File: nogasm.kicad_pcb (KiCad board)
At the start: 2 copper layers, 76.2 x 76.2 mm, 57 parts, among them J1 PJ-031DH 3.5mm, J2 PRT-10811, Q1 BUK92150-55A, Q2 MMBT2222A, Q3 MMBT2222A, Q4 MMBT2222A, SW1 SW_DIP_x04, U1 WS2812B, U10 WS2812B, U11 WS2812B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

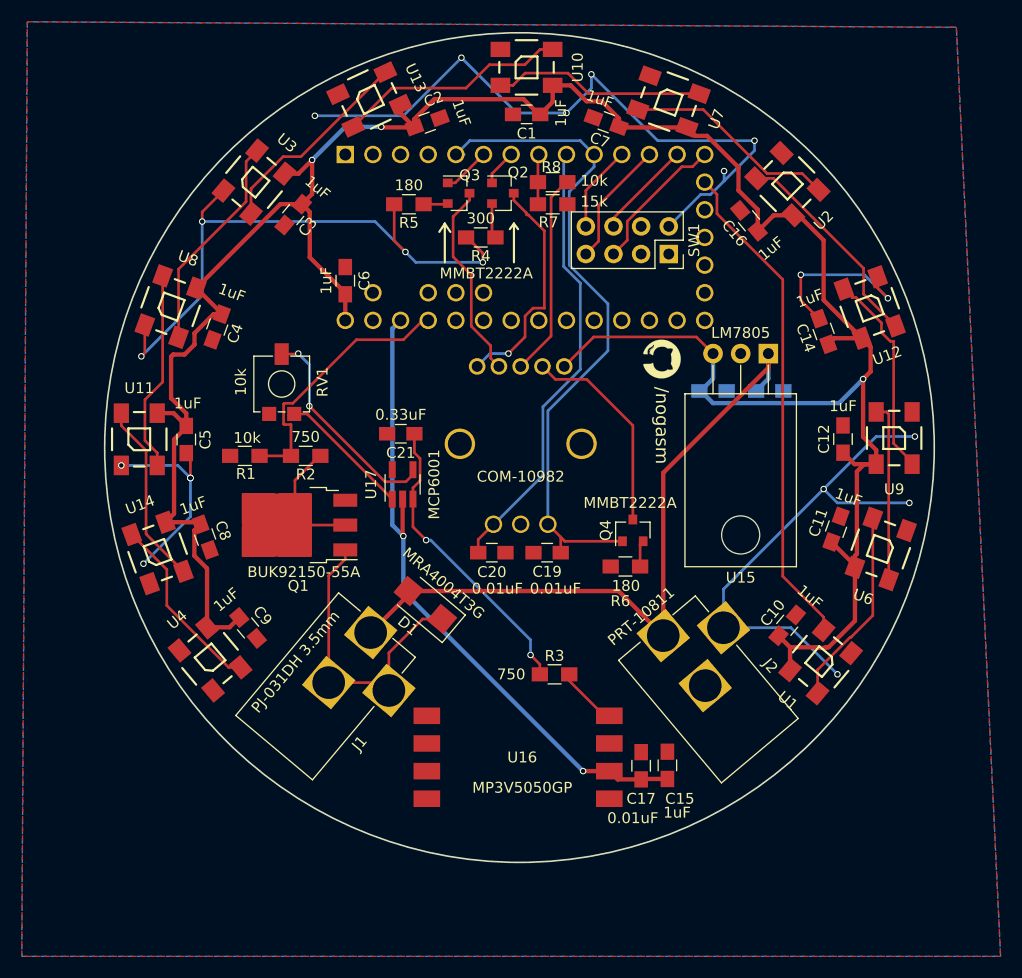
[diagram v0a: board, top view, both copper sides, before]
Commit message: changing DIP switch to SMD and fixing some library linking
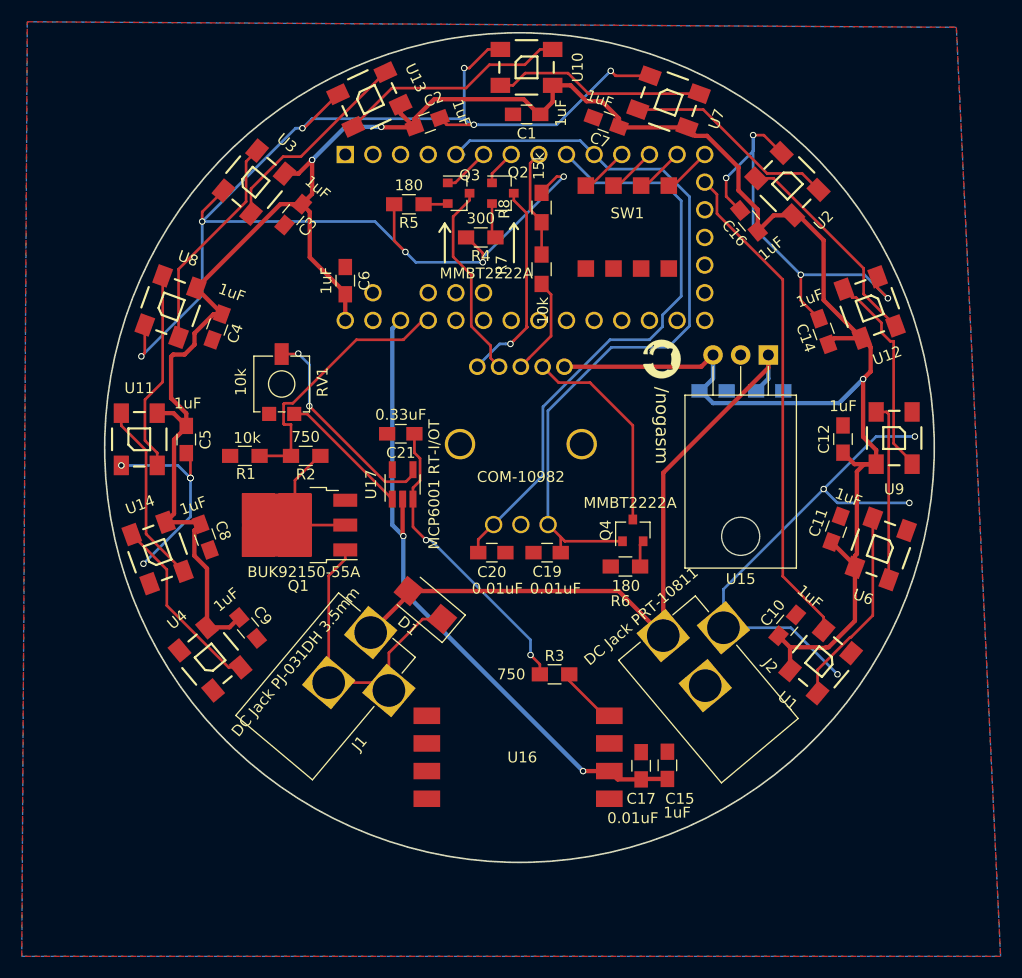
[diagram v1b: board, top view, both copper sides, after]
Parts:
- D1: footprint sma:D_SMA_0202 -> nogasm:D_SMA_0202
- J1: value PJ-031DH 3.5mm -> DC Jack PJ-031DH 3.5mm
- J2: value PRT-10811 -> DC Jack PRT-10811
- SW1: footprint Socket_Strips:Socket_Strip_Straight_2x04_Pitch2.54mm -> nogasm:SW_DIP_4_SMD
- U15: value LM7805 -> LM7805CT
- U16: footprint sma:MP3V5050GP -> nogasm:MP3V5050GP
- U17: value MCP6001 -> MCP6001 RT-I/OT
- U5: footprint sma:Teensy30_31_32_LC -> nogasm:Teensy30_31_32_LC
- moved R7 8.07 mm to (121.9, 69.0), turned to 90 degrees
- moved SW1 4.54 mm to (129.8, 65.1), turned to 180 degrees
- moved R8 1.06 mm to (121.9, 63.3), turned to 90 degrees
- moved U15 0.13 mm to (142.7, 76.8)
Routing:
- net GND: track 201.2 -> 243.6 mm, vias 20 -> 21
- net /ENC_A: track 41.2 -> 54.5 mm
- net /ENC_B: track 62.1 -> 72.3 mm
- net Net-(R7-Pad1): track 18.8 -> 9.09 mm
- net Net-(SW1-Pad5): track 13.2 -> 4.49 mm
- net Net-(SW1-Pad7): track 11.6 -> 4.49 mm
- net /ENC_SW: track 4.61 -> 10.4 mm
- net Net-(SW1-Pad6): track 9.02 -> 4.61 mm
- net Net-(SW1-Pad8): track 7.97 -> 4.49 mm
- net Net-(Q2-Pad3): track 21.3 -> 18.9 mm
- net +5V: track 240.6 -> 239.6 mm
